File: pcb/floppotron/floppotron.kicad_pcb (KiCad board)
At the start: 2 copper layers, 100 x 92 mm, 62 parts, among them J1 DIN-5_180degree, J10 Power, J2 Conn_01x02, J3 Conn_01x02, J4 Conn_01x02, J5 Conn_01x02, J6 Conn_01x02, J7 Conn_01x02, J9 USB_B, Q1 BC817, Q11 BC817, Q12 BC817, Q14 BC817, Q15 BC817, Q16 BC817, Q17 BC817, Q18 BC817, Q19 BC817, Q2 BC817, Q20 BC817, Q3 BC817, Q4 BC817, Q5 BC817, Q6 BC817, Q7 BC817, Q8 BC817, Q9 BC817, U1 H11L1, U2 Pico

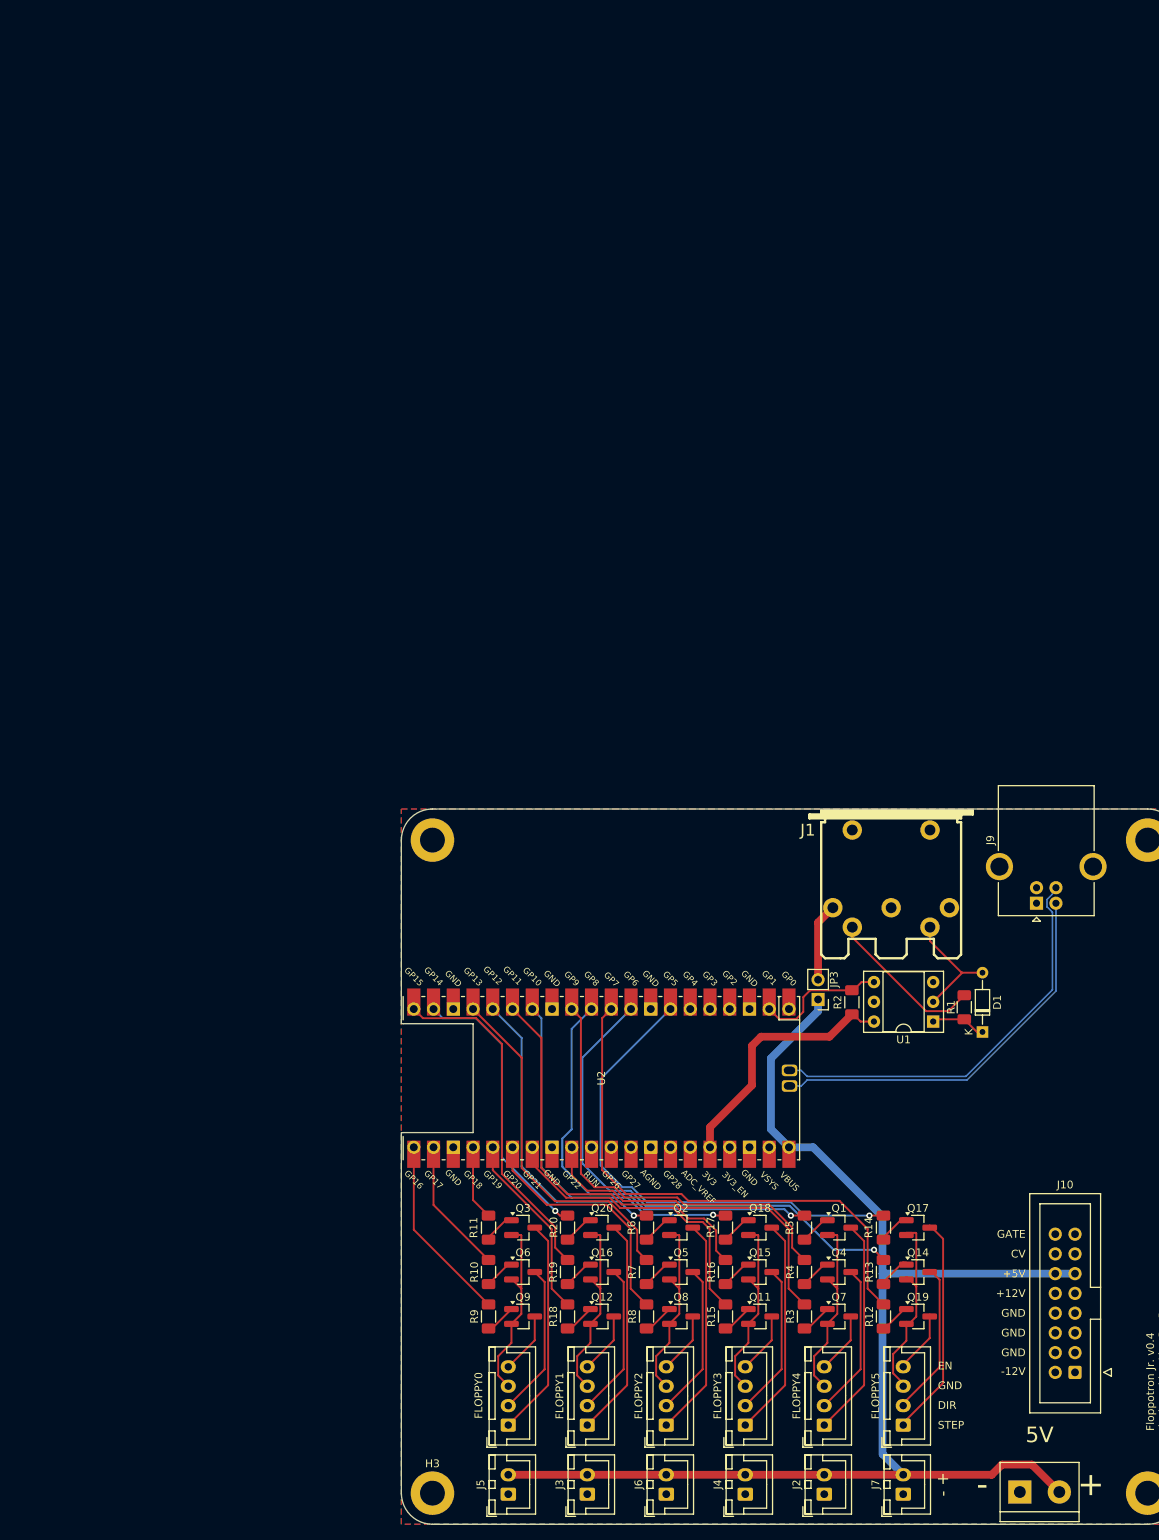
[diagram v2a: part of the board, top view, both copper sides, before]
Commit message: clean up traces
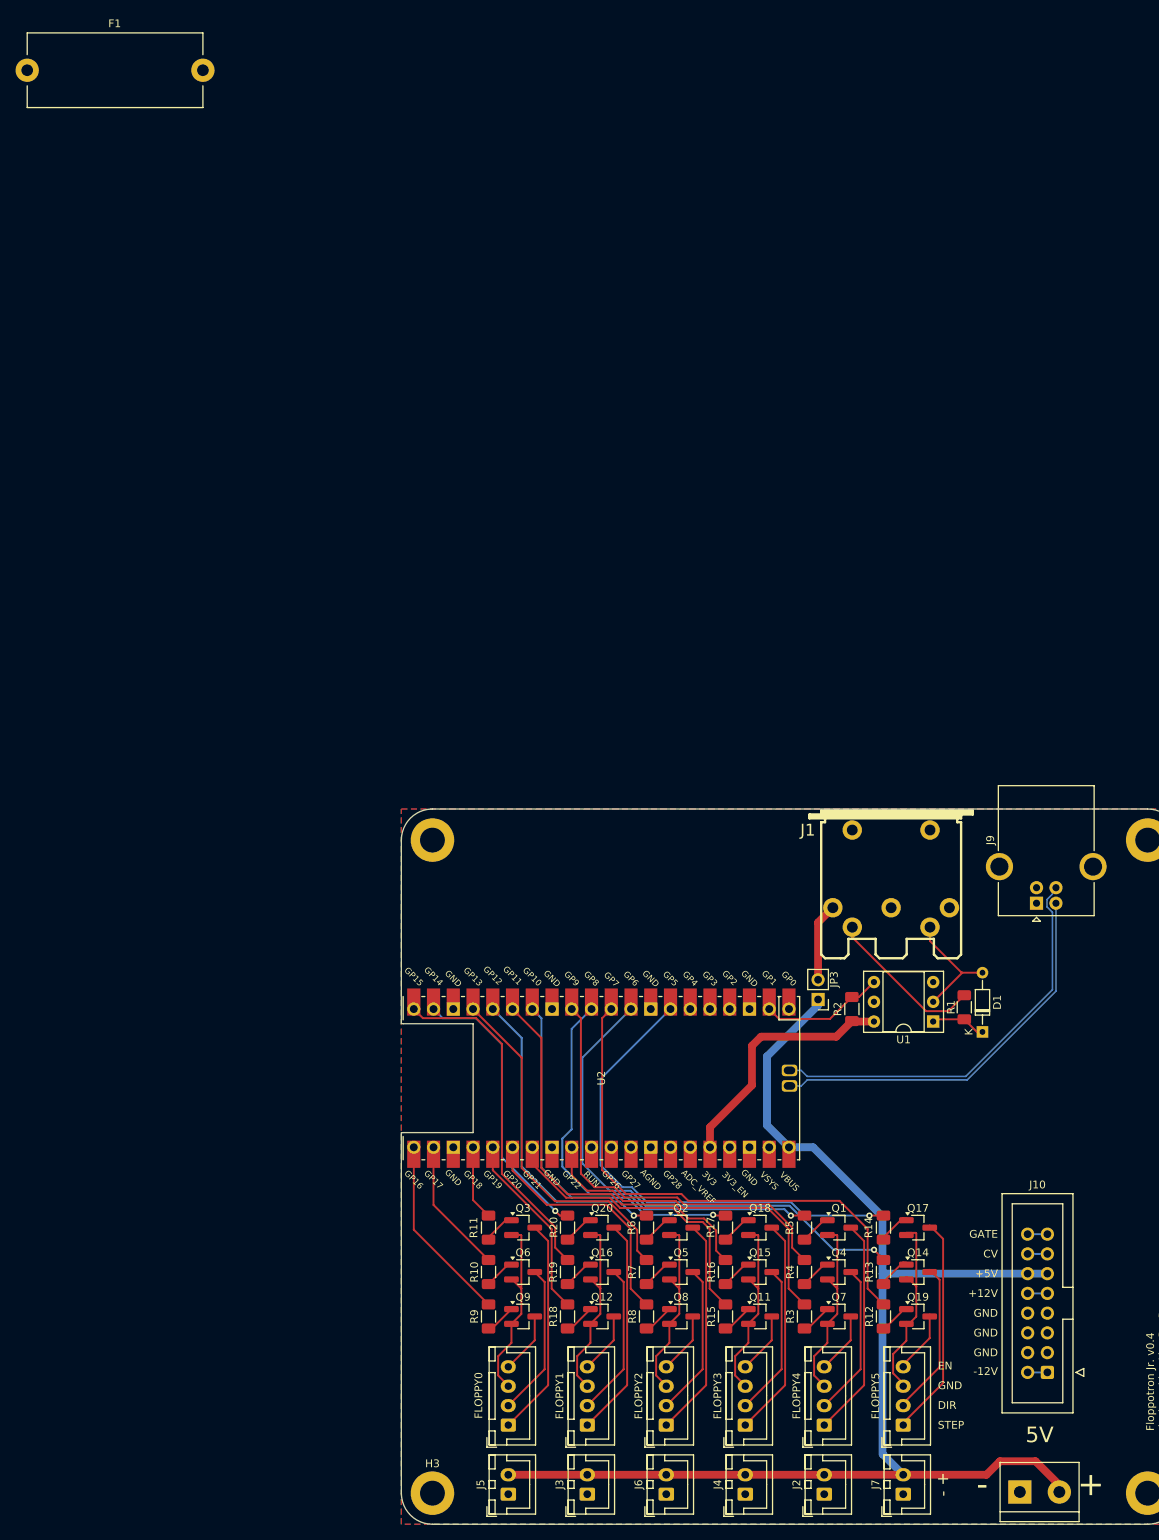
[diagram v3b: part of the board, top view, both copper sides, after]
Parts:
- added F1: Fuse, Fuse:Fuseholder_Cylinder-5x20mm_Stelvio-Kontek_PTF78_Horizontal_Open, F.Cu at (1.88, 4.97)
- moved J10 3.56 mm to (131.8, 163.6)
- moved R2 0.87 mm to (108.0, 125.7)
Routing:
- net unconnected-(J10-GATE-Pad6): track 0.00 -> 2.54 mm
- net unconnected-(J10-CV-Pad5): track 0.00 -> 2.54 mm
- net unconnected-(J10--12V-Pad1): track 0.00 -> 2.54 mm
- net unconnected-(J10-+12V-Pad3): track 0.00 -> 2.54 mm
- net VCC: track 170.2 -> 167.9 mm
- net MIDI IN: track 16.6 -> 16.0 mm
- net +3V3: track 32.8 -> 32.3 mm

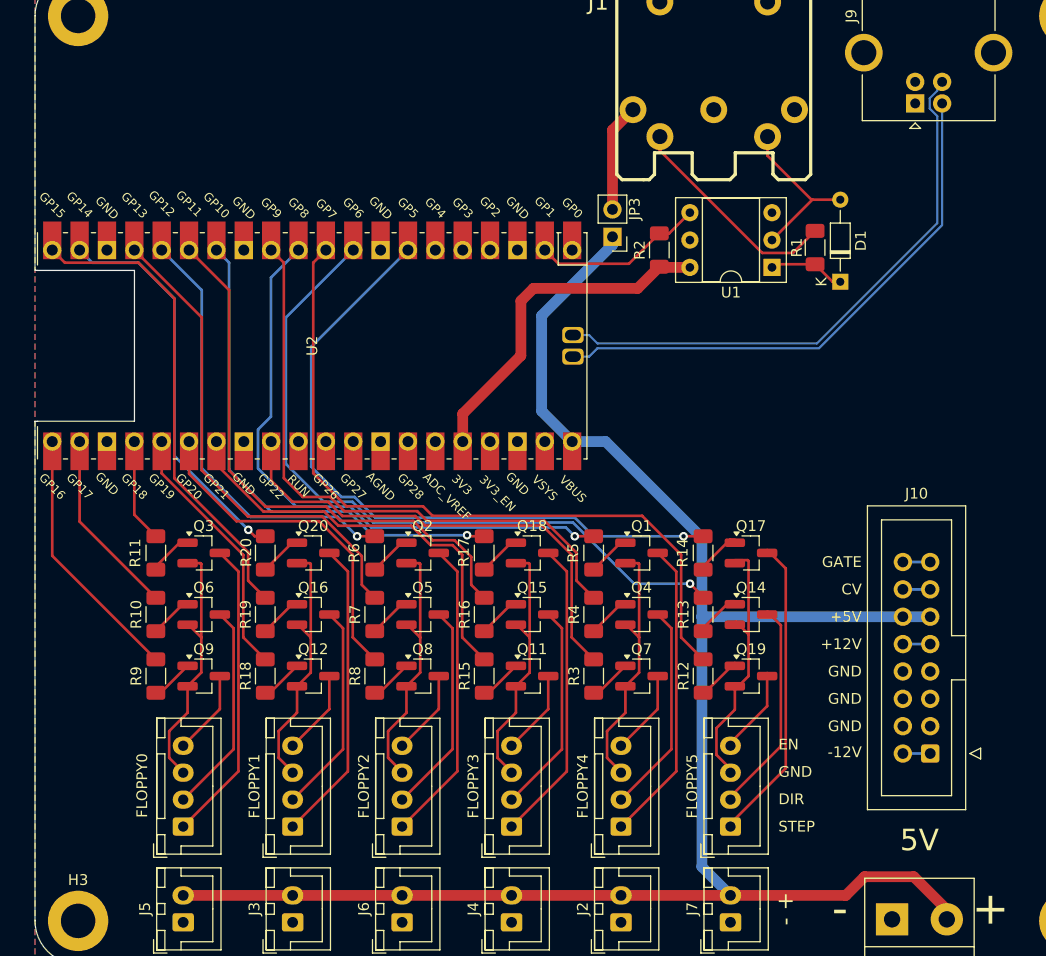
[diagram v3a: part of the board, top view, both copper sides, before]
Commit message: pcb: adapt for interface board
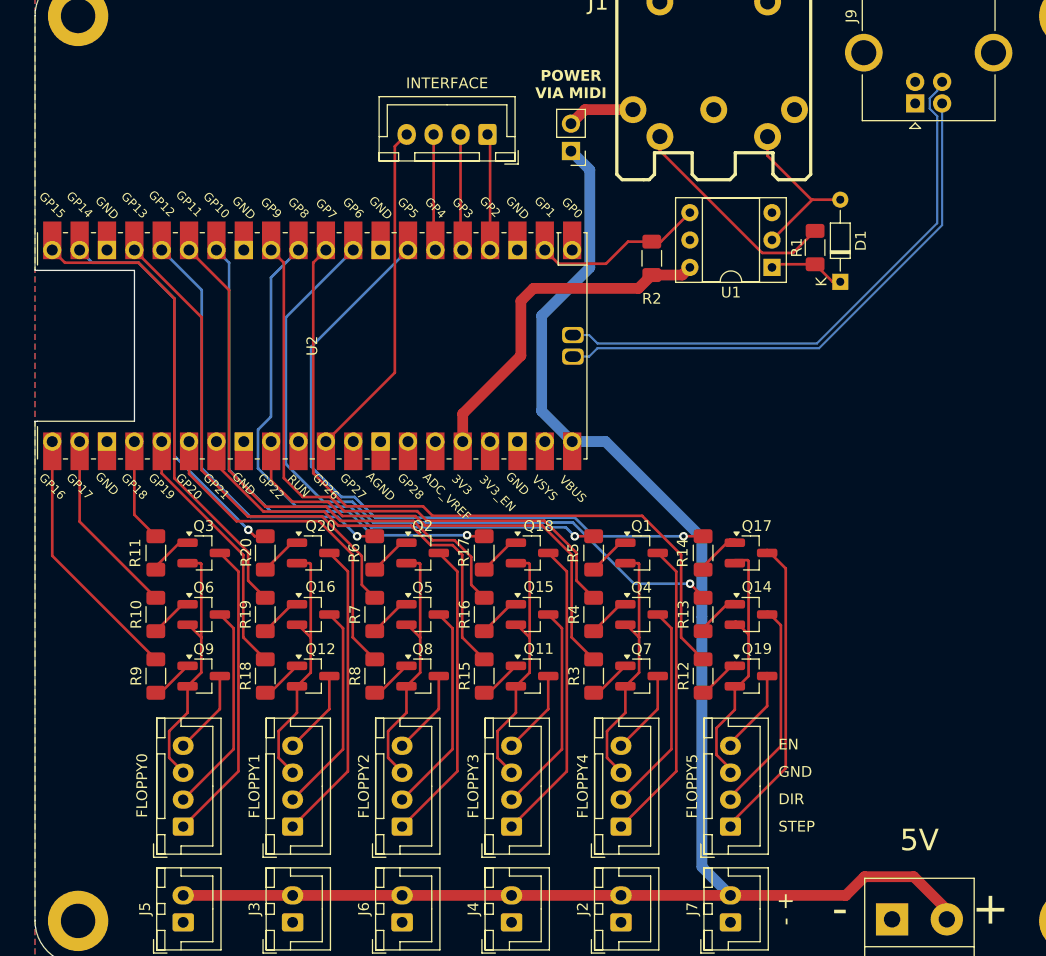
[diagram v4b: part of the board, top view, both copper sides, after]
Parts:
- removed J10: Power, kosmo:Power 16 Pin
- added INTERFACE: Conn_01x04, Connector_JST:JST_XH_B4B-XH-A_1x04_P2.50mm_Vertical, F.Cu at (92.0, 115.0)
- moved JP3 8.84 mm to (99.8, 116.5)
- moved R2 1.04 mm to (107.2, 126.5)
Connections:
- U2 pad 31: unconnected-(U2-GPIO26_ADC0-Pad31) -> GATE
- U2 pad 4: unconnected-(U2-GPIO2-Pad4) -> MOD
- U2 pad 5: unconnected-(U2-GPIO3-Pad5) -> VEL
- U2 pad 6: unconnected-(U2-GPIO4-Pad6) -> TRIG
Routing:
- net GATE: track 0.00 -> 31.6 mm
- net VCC: track 167.9 -> 154.5 mm
- net MOD: track 0.00 -> 10.8 mm
- net VEL: track 0.00 -> 10.8 mm
- net TRIG: track 0.00 -> 10.8 mm
- net /VCC_device: track 10.1 -> 6.29 mm
- net unconnected-(J10-GATE-Pad6): track 2.54 -> 0.00 mm
- net unconnected-(J10-CV-Pad5): track 2.54 -> 0.00 mm
- net unconnected-(J10--12V-Pad1): track 2.54 -> 0.00 mm
- net unconnected-(J10-+12V-Pad3): track 2.54 -> 0.00 mm
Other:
- board text added: "POWER VIA MIDI"
